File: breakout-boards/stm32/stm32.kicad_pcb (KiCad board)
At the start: 2 copper layers, 34.3 x 71.2 mm, 41 parts, among them J1 Conn_ARM_JTAG_SWD_10, J2 AudioJack4, J3 CONN_LEFT, J4 CONN_RIGHT, J5 USB_SENSE, P1 USB_C, Q1 Q_NPN_BEC, Q2 Q_NPN_BEC, SW1 RST_SW, U1 AP2127N-3.3, U2 STM32F042K6Tx, Y1 16MHz

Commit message: (#2) generate gerbers
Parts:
- removed the G*** at (124.1, 91.7)
- removed the G*** at (125.2, 80.6)

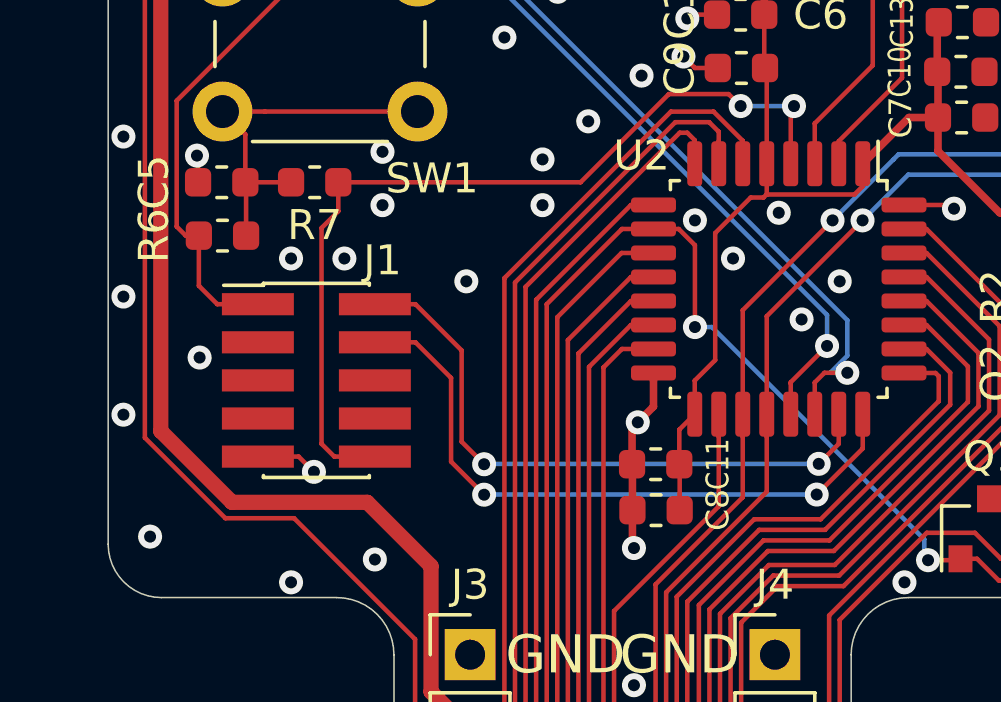
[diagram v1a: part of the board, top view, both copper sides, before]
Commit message: switch jtag header from smd to pth
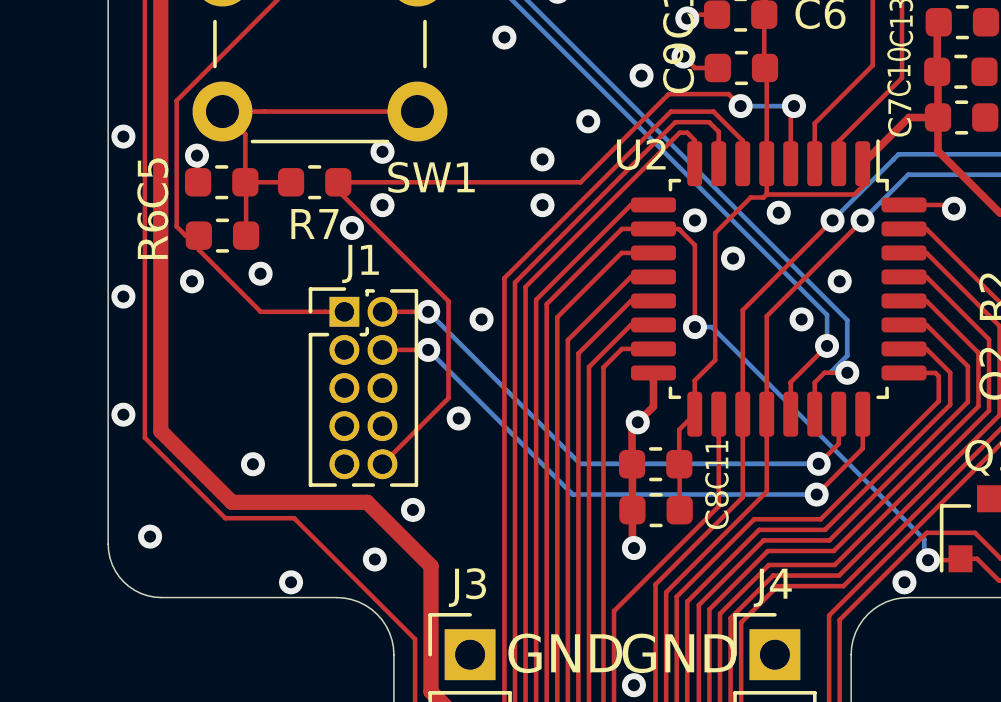
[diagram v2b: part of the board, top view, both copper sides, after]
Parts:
- J1: footprint Connector_PinHeader_1.27mm:PinHeader_2x05_P1.27mm_Vertical_SMD -> Connector_PinHeader_1.27mm:PinHeader_2x05_P1.27mm_Vertical
- moved J1 2.47 mm to (118.4, 90.2)
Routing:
- net +3V3: track 95.6 -> 97.9 mm
- net /SWDIO: track 20.7 -> 18.6 mm
- net GND: track 28.2 -> 26.2 mm, vias 96 -> 98
- net /SWCLK: track 21.8 -> 19.8 mm
- net /nRST: track 29.4 -> 30.4 mm
